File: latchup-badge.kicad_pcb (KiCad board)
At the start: 2 copper layers, 101.6 x 71.1 mm, 18 parts, among them U1 ICE40UP5K-SG48ITR, U2 TLV70012_SOT23-5, U3 TLV70033_SOT23-5

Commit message: Moar updates
Signed-off-by: Michael Welling <mwelling@ieee.org>
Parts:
- added C14: .1uF, Capacitor_SMD:C_0402_1005Metric, F.Cu at (144.1, 60.8)
- added C15: .1uF, Capacitor_SMD:C_0402_1005Metric, F.Cu at (130.8, 76.7)
- added R2: 10K, Resistor_SMD:R_0402_1005Metric, F.Cu at (141.5, 58.3)
- added U4: M25PX32-VMW, Package_SO:SOIJ-8_5.3x5.3mm_P1.27mm, F.Cu at (124.0, 79.2)
- added X1: ASE-12.000MHz, Oscillator:Oscillator_SMD_Abracon_ASE-4Pin_3.2x2.5mm, F.Cu at (141.2, 60.8)

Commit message: Add some artwork
Signed-off-by: Michael Welling <mwelling@ieee.org>
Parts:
- added G***: LOGO, latchup-badge:logo_1, F.Cu at (127.0, 104.1)
- added G***: LOGO, latchup-badge:logo, F.Cu at (127.0, 104.1)
- added J1: USB_B_Micro, Connector_USB:USB_Micro-B_Molex-105017-0001, B.Cu at (79.3, 78.2)
- added R3: 25, Resistor_SMD:R_0402_1005Metric, B.Cu at (85.0, 77.9)
- added R4: 25, Resistor_SMD:R_0402_1005Metric, B.Cu at (85.0, 78.9)
- added R5: 1.5K, Resistor_SMD:R_0402_1005Metric, B.Cu at (106.0, 68.3)
- C1, C10, C11, C12, C13, C14, C15, C2, C3, C4, C5, C6, C7, C8, C9, D1, R1, R2, U1, U2, U3, U4, X1: moved to B.Cu
- moved C8 43.3 mm to (98.0, 68.4), turned to 180 degrees
- moved C14 42.8 mm to (101.4, 59.9)
- moved C7 42.3 mm to (98.9, 65.6), turned to 180 degrees
- moved R2 37.5 mm to (104.0, 57.3), turned to 0 degrees
- moved C9 37.0 mm to (104.3, 65.7), turned to 180 degrees
- moved X1 37.0 mm to (104.3, 59.8), turned to 0 degrees
- moved C3 37.0 mm to (104.3, 63.8), turned to 0 degrees
- moved C10 37.0 mm to (104.3, 68.4), turned to 180 degrees
- moved R1 37.0 mm to (104.3, 67.4), turned to 180 degrees
- moved D1 30.1 mm to (107.7, 72.6)
- moved C5 29.8 mm to (93.3, 85.9), turned to 0 degrees
- moved U3 29.8 mm to (93.3, 82.7)
- moved C2 29.8 mm to (93.3, 79.5), turned to 0 degrees
- moved C6 27.1 mm to (109.2, 72.6)
- moved U1 23.4 mm to (111.1, 66.0), turned to 180 degrees
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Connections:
- U1 pad 14: Net-(U1-Pad14) -> /ICE40_SPI_SO
- U1 pad 15: Net-(U1-Pad15) -> /ICE40_SPI_SCK
- U1 pad 16: Net-(U1-Pad16) -> /ICE40_SPI_SS
- U1 pad 17: Net-(U1-Pad17) -> /ICE40_SPI_SI
- U4 pad 1: Net-(U4-Pad1) -> /ICE40_SPI_SS
- U4 pad 2: Net-(U4-Pad2) -> /ICE40_SPI_SI
- U4 pad 5: Net-(U4-Pad5) -> /ICE40_SPI_SO
- U4 pad 6: Net-(U4-Pad6) -> /ICE40_SPI_SCK
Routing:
- net +3V3: track 0.00 -> 1.74 mm, vias 0 -> 1
- added copper zone on F.Cu, net +3V3
- added copper zone on B.Cu, net GND
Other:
- board text added: "HELLO"
- board text added: "MY NAME IS"

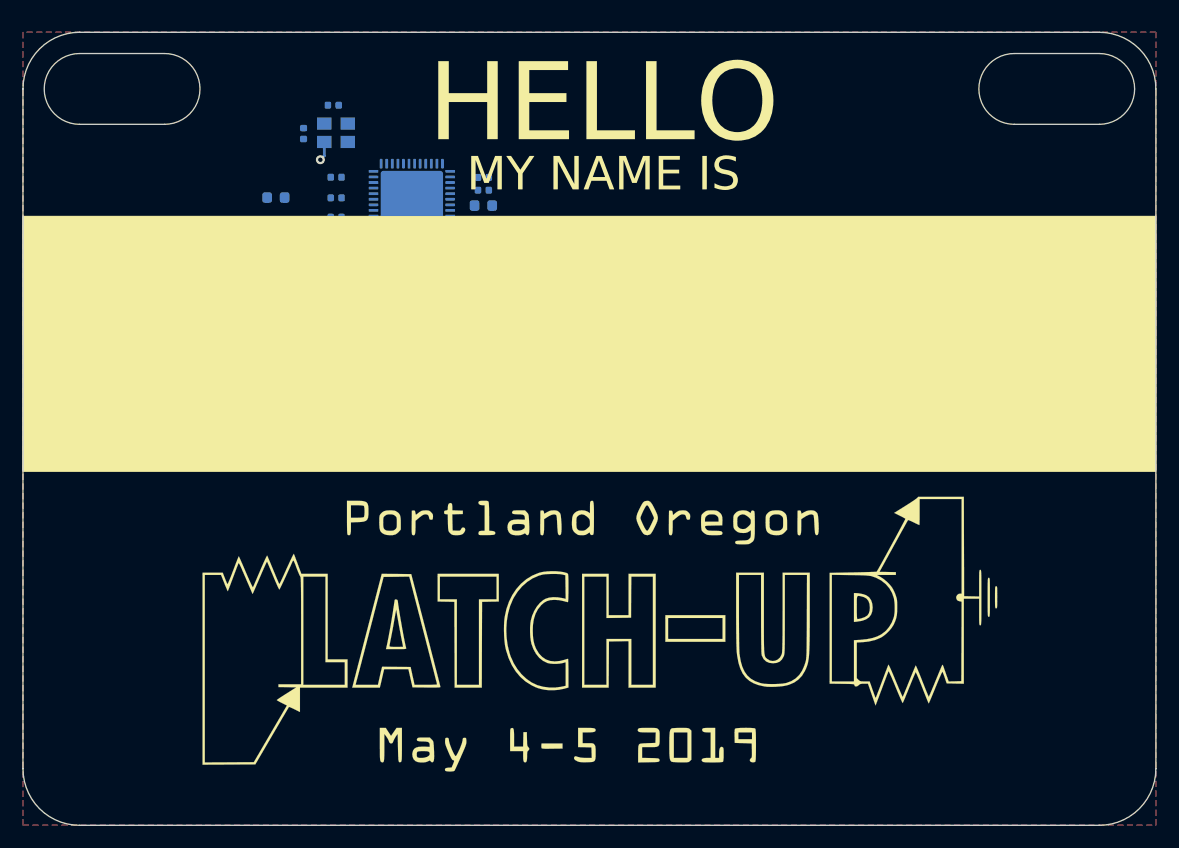
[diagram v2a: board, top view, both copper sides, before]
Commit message: Add some headers and route
Some small tweaks left but mostly done.

Signed-off-by: Michael Welling <mwelling@ieee.org>
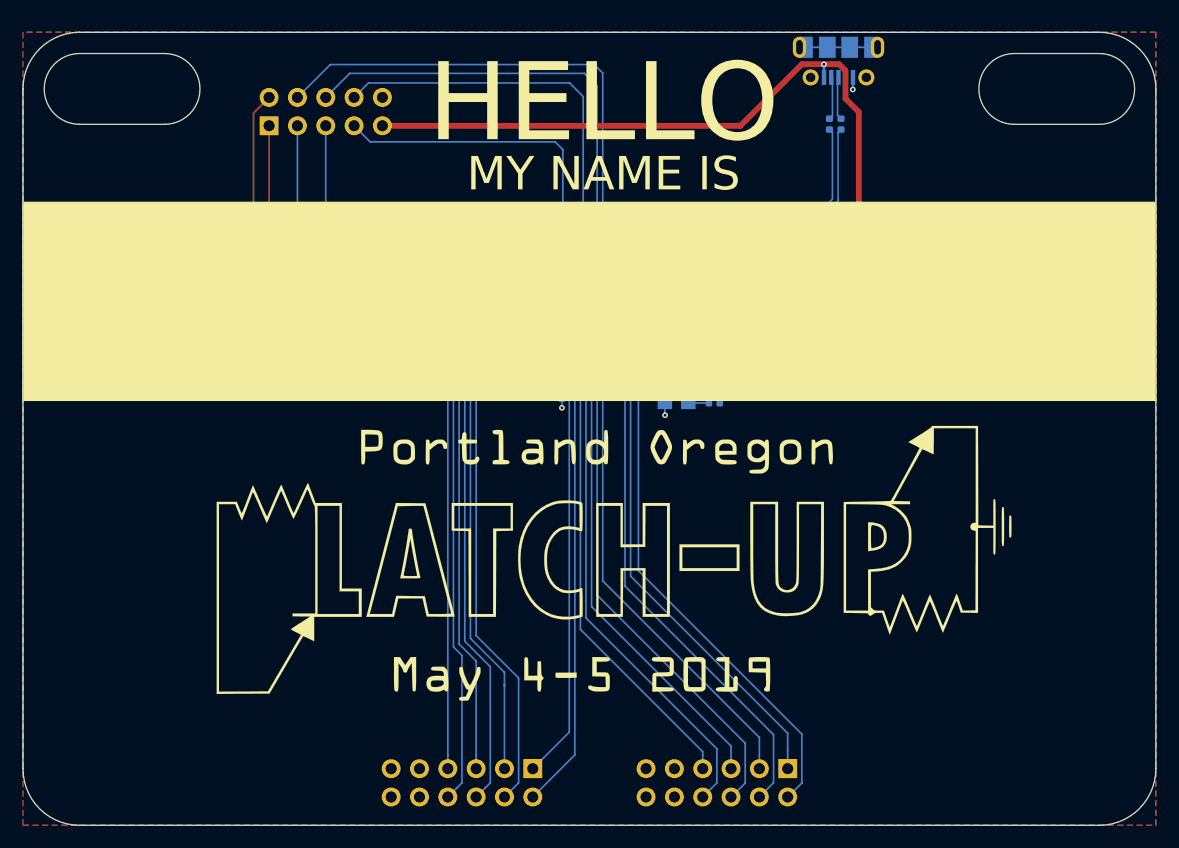
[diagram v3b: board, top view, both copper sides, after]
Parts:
- added J2: CONN_02X06, Connector_PinSocket_2.54mm:PinSocket_2x06_P2.54mm_Horizontal, B.Cu at (144.8, 116.8)
- added J3: CONN_02X06, Connector_PinSocket_2.54mm:PinSocket_2x06_P2.54mm_Horizontal, B.Cu at (121.9, 116.8)
- added J4: CONN_02X05, Connector_PinSocket_2.54mm:PinSocket_2x05_P2.54mm_Vertical, B.Cu at (98.3, 59.2)
- moved J1 74.3 mm to (149.3, 53.4), turned to 0 degrees
- moved R3 67.3 mm to (149.6, 59.0), turned to 90 degrees
- moved R4 66.6 mm to (148.5, 59.0), turned to 90 degrees
- moved C2 56.5 mm to (149.5, 73.8), turned to 270 degrees
- moved U3 53.7 mm to (146.3, 73.9), turned to 180 degrees
- moved C5 51.3 mm to (143.1, 73.9), turned to 270 degrees
- moved C1 49.9 mm to (149.5, 80.2), turned to 270 degrees
- moved U2 46.7 mm to (146.3, 80.3), turned to 180 degrees
- moved C4 43.9 mm to (143.1, 80.3), turned to 270 degrees
- moved R2 43.4 mm to (138.2, 84.0)
- moved C14 43.3 mm to (138.4, 82.4), turned to 180 degrees
- moved C7 42.1 mm to (139.3, 77.5), turned to 0 degrees
- moved C8 41.9 mm to (139.3, 75.6), turned to 0 degrees
- moved X1 38.5 mm to (134.8, 83.2), turned to 180 degrees
- moved C3 34.3 mm to (134.7, 79.5), turned to 180 degrees
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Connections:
- net Net-(R?1555303253-Pad1) renamed /USBD+
- net Net-(R?1555309571-Pad1) renamed /USBD-
- R5 pad 1: Net-(U1-Pad25) -> Net-(R5-Pad1)
- U1 pad 10: Net-(U1-Pad10) -> /J3_P6
- U1 pad 11: Net-(U1-Pad11) -> /J3_P5
- U1 pad 12: Net-(U1-Pad12) -> /J3_P8
- U1 pad 13: Net-(U1-Pad13) -> /J3_P7
- U1 pad 18: Net-(U1-Pad18) -> /RX
- U1 pad 19: Net-(U1-Pad19) -> /TX
- U1 pad 28: Net-(U1-Pad28) -> Net-(R5-Pad1)
- U1 pad 36: Net-(U1-Pad36) -> /J2_P2
- U1 pad 37: Net-(U1-Pad37) -> /J2_P1
- U1 pad 38: Net-(U1-Pad38) -> /J2_P4
- U1 pad 42: Net-(U1-Pad42) -> /J2_P3
- U1 pad 43: Net-(U1-Pad43) -> /J2_P6
- U1 pad 44: Net-(U1-Pad44) -> /J2_P5
- U1 pad 45: Net-(U1-Pad45) -> /J2_P8
- U1 pad 46: Net-(U1-Pad46) -> /J2_P7
- U1 pad 47: Net-(U1-Pad47) -> /J3_P2
- U1 pad 48: Net-(U1-Pad48) -> /J3_P1
- U1 pad 6: Net-(U1-Pad6) -> /J3_P4
- U1 pad 7: Net-(U1-Pad7) -> /CDONE
- U1 pad 8: Net-(U1-Pad8) -> /CRESET
- U1 pad 9: Net-(U1-Pad9) -> /J3_P3
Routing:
- net +5V: track 0.00 -> 80.2 mm, vias 0 -> 5
- net /J3_P8: track 0.00 -> 54.4 mm
- net /J3_P6: track 0.00 -> 53.0 mm
- net /J3_P7: track 0.00 -> 52.9 mm
- net /J3_P5: track 0.00 -> 50.6 mm
- net /J3_P4: track 0.00 -> 50.6 mm
- net /J3_P3: track 0.00 -> 49.4 mm
- net /TX: track 0.00 -> 49.0 mm
- net /CDONE: track 0.00 -> 48.3 mm, vias 0 -> 1
- net /ICE40_SPI_SI: track 0.00 -> 45.8 mm
- net /J2_P2: track 0.00 -> 45.3 mm
- net /RX: track 0.00 -> 44.6 mm
- net /J2_P4: track 0.00 -> 44.0 mm
- net /J2_P6: track 0.00 -> 44.0 mm
- net /CRESET: track 0.00 -> 43.4 mm, vias 0 -> 1
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- added copper zone on B.Cu, net +3V3
- added copper zone on F.Cu, net GND
- removed copper zone on F.Cu, net +3V3
- removed copper zone on B.Cu, net GND
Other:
- net class Default: clearance 0.2 -> 0.1524; trace_width 0.25 -> 0.1524; via_dia 0.8 -> 0.508; via_drill 0.4 -> 0.254
- rule trace_clearance: 0.2 -> 0.1524
- rule trace_min: 0.2 -> 0.1524
- rule via_min_drill: 0.3 -> 0.254
- rule via_min_size: 0.4 -> 0.508

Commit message: OSHPark is sponsoring the PCBs!
Signed-off-by: Michael Welling <mwelling@ieee.org>
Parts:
- added G***: LOGO, latchup-badge:logo_3, B.Cu at (106.9, 101.8)
- added G***: KiCad Logo, latchup-badge:KiCad-Logo_Copper_11mmx5mm, F.Cu at (90.6, 117.9)
- added G***: LOGO, latchup-badge:logo_2, B.Cu at (159.0, 102.2)
- added R6: 10K, Resistor_SMD:R_0402_1005Metric, B.Cu at (98.2, 62.5)
- added R7: 10K, Resistor_SMD:R_0402_1005Metric, B.Cu at (124.2, 64.8)
- added R8: 10K, Resistor_SMD:R_0402_1005Metric, B.Cu at (114.2, 68.4)
- added R9: 10K, Resistor_SMD:R_0402_1005Metric, B.Cu at (126.8, 69.2)
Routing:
- net /CRESET: track 43.4 -> 46.3 mm
- net Net-(R8-Pad1): track 0.00 -> 2.61 mm
- net Net-(R9-Pad1): track 0.00 -> 2.15 mm
- net /RX: track 44.6 -> 46.3 mm
- net /TX: track 49.0 -> 50.5 mm
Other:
- board text added: "PCB Sponsored by:"
- board text added: "m_w"

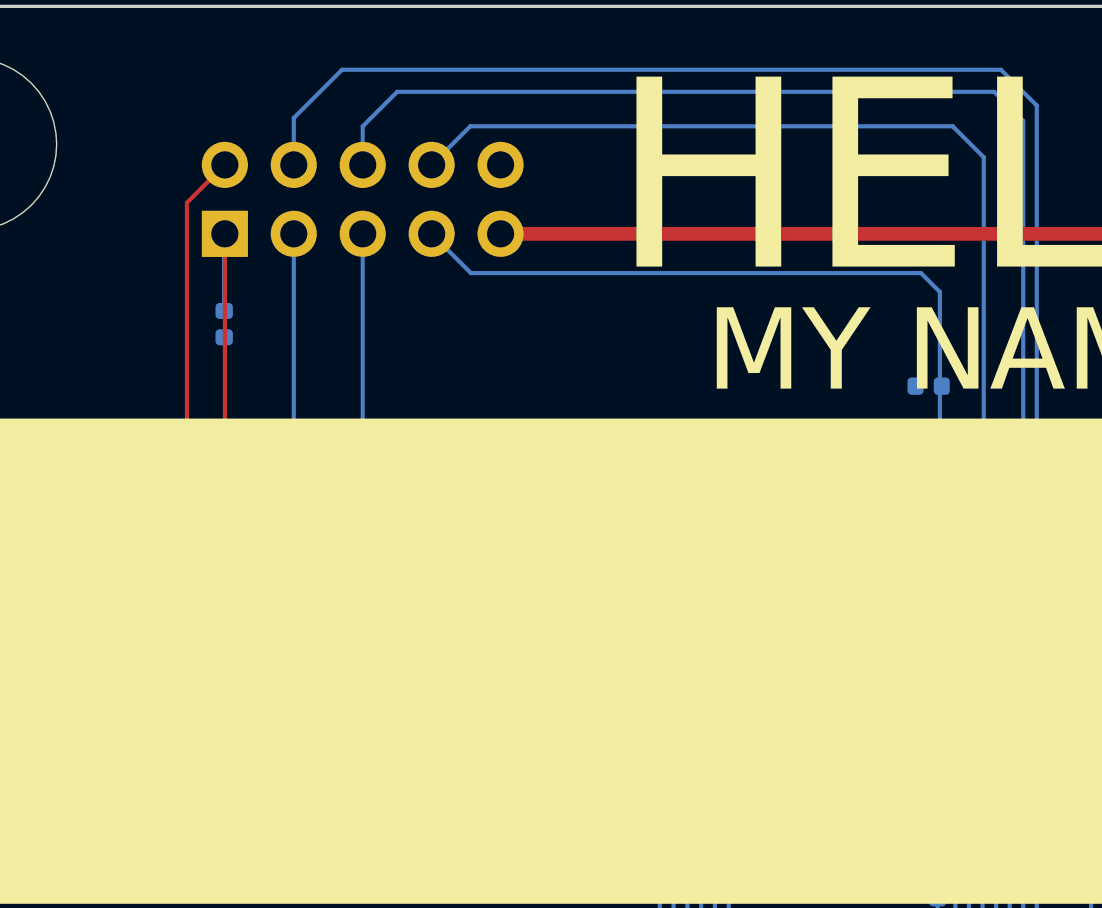
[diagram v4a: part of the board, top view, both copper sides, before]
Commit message: Tweak routing per review from tnt
Gives the GND plane more room to breathe.

Signed-off-by: Michael Welling <mwelling@ieee.org>
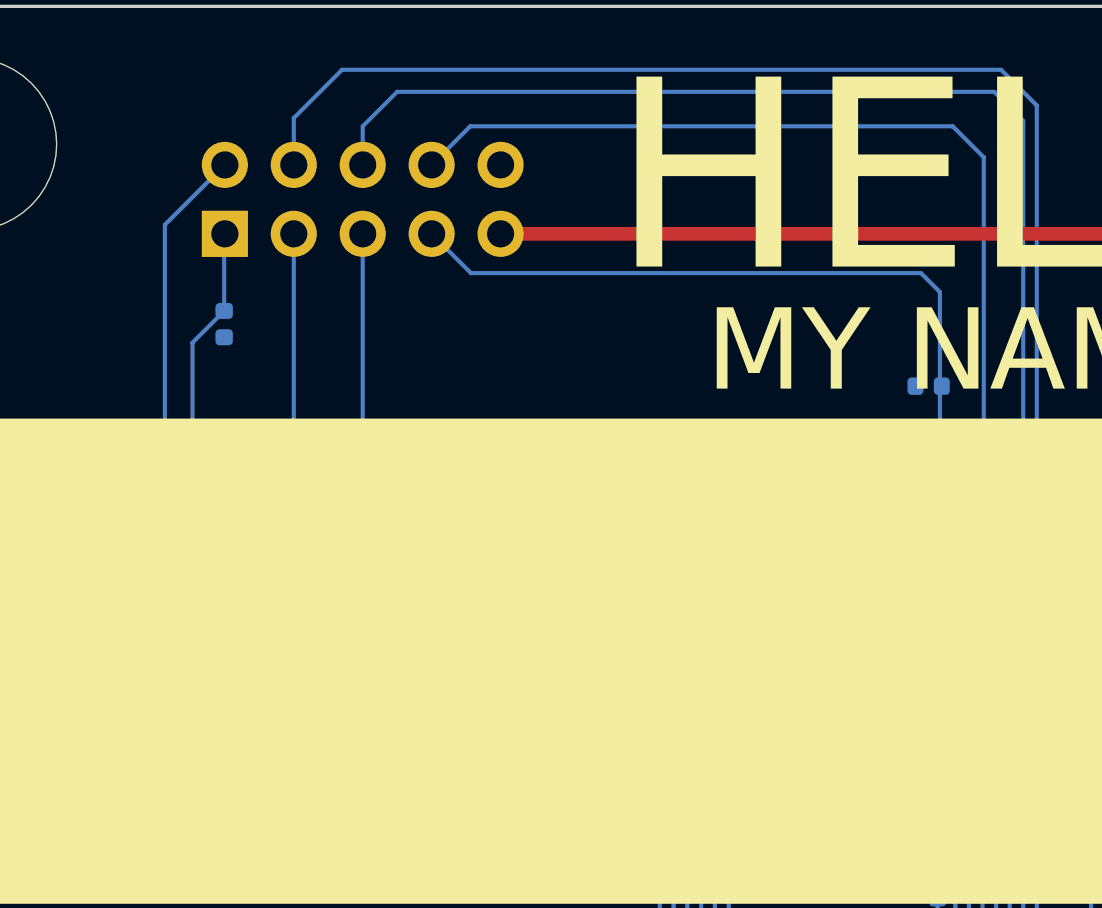
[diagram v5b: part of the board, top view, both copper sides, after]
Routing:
- net /CRESET: track 46.3 -> 42.8 mm, vias 1 -> 2
- net /CDONE: track 48.3 -> 47.2 mm, vias 1 -> 2
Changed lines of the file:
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@@
     (thickness 1.6)
     (drawings 21)
-    (tracks 328)
+    (tracks 334)
     (zones 0)
     (modules 39)
@@
   (segment (start 100.8126 54.9148) (end 102.5906 53.1368) (width 0.1524) (layer "B.Cu") (net 51))
   (segment (start 100.8126 56.642) (end 100.8126 54.9148) (width 0.1524) (layer "B.Cu") (net 51))
-  (via (at 123.0122 77.761554) (size 0.508) (drill 0.254) (layers "F.Cu" "B.Cu") (net 52))
-  (segment (start 124.486971 77.761554) (end 123.0122 77.761554) (width 0.1524) (layer "B.Cu") (net 52))
-  (segment (start 124.504371 77.744154) (end 124.486971 77.761554) (width 0.1524) (layer "B.Cu") (net 52))
-  (segment (start 96.8756 58.039) (end 97.422601 57.491999) (width 0.1524) (layer "F.Cu") (net 52))
-  (segment (start 97.422601 57.491999) (end 98.2726 56.642) (width 0.1524) (layer "F.Cu") (net 52))
-  (segment (start 96.8756 76.0476) (end 96.8756 58.039) (width 0.1524) (layer "F.Cu") (net 52))
-  (segment (start 98.589554 77.761554) (end 96.8756 76.0476) (width 0.1524) (layer "F.Cu") (net 52))
-  (segment (start 123.0122 77.761554) (end 98.589554 77.761554) (width 0.1524) (layer "F.Cu") (net 52))
-  (via (at 123.4694 77.2668) (size 0.508) (drill 0.254) (layers "F.Cu" "B.Cu") (net 53))
-  (segment (start 123.492046 77.244154) (end 123.4694 77.2668) (width 0.1524) (layer "B.Cu") (net 53))
-  (segment (start 124.504371 77.244154) (end 123.492046 77.244154) (width 0.1524) (layer "B.Cu") (net 53))
-  (segment (start 98.2726 75.692) (end 98.2726 59.182) (width 0.1524) (layer "F.Cu") (net 53))
-  (segment (start 99.5426 76.962) (end 98.2726 75.692) (width 0.1524) (layer "F.Cu") (net 53))
-  (segment (start 123.1646 76.962) (end 99.5426 76.962) (width 0.1524) (layer "F.Cu") (net 53))
-  (segment (start 123.4694 77.2668) (end 123.1646 76.962) (width 0.1524) (layer "F.Cu") (net 53))
+  (segment (start 124.486971 77.761554) (end 124.504371 77.744154) (width 0.1524) (layer "B.Cu") (net 52))
+  (segment (start 116.904046 77.761554) (end 124.486971 77.761554) (width 0.1524) (layer "B.Cu") (net 52))
+  (via (at 116.904046 77.761554) (size 0.508) (drill 0.254) (layers "F.Cu" "B.Cu") (net 52))
+  (via (at 112.903 73.7362) (size 0.508) (drill 0.254) (layers "F.Cu" "B.Cu") (net 52))
+  (segment (start 116.904046 77.761554) (end 112.903 73.760508) (width 0.1524) (layer "F.Cu") (net 52))
+  (segment (start 112.54379 73.7362) (end 112.903 73.7362) (width 0.1524) (layer "B.Cu") (net 52))
+  (segment (start 112.903 73.760508) (end 112.903 73.7362) (width 0.1524) (layer "F.Cu") (net 52))
+  (segment (start 98.2726 56.642) (end 96.0628 58.8518) (width 0.1524) (layer "B.Cu") (net 52))
+  (segment (start 96.0628 58.8518) (end 96.0628 72.2122) (width 0.1524) (layer "B.Cu") (net 52))
+  (segment (start 97.5868 73.7362) (end 112.54379 73.7362) (width 0.1524) (layer "B.Cu") (net 52))
+  (segment (start 96.0628 72.2122) (end 97.5868 73.7362) (width 0.1524) (layer "B.Cu") (net 52))
   (segment (start 98.2472 59.2074) (end 98.2726 59.182) (width 0.1524) (layer "B.Cu") (net 53))
   (segment (start 98.2472 62.0244) (end 98.2472 59.2074) (width 0.1524) (layer "B.Cu") (net 53))
+  (segment (start 124.504371 77.244154) (end 117.573846 77.244154) (width 0.1524) (layer "B.Cu") (net 53))
+  (segment (start 117.573846 77.244154) (end 117.5512 77.2668) (width 0.1524) (layer "B.Cu") (net 53))
+  (via (at 117.5512 77.2668) (size 0.508) (drill 0.254) (layers "F.Cu" "B.Cu") (net 53))
+  (via (at 113.3856 73.1012) (size 0.508) (drill 0.254) (layers "F.Cu" "B.Cu") (net 53))
+  (segment (start 117.5512 77.2668) (end 113.3856 73.1012) (width 0.1524) (layer "F.Cu") (net 53))
+  (segment (start 113.02639 73.1012) (end 113.3856 73.1012) (width 0.1524) (layer "B.Cu") (net 53))
+  (segment (start 98.4758 73.1012) (end 113.02639 73.1012) (width 0.1524) (layer "B.Cu") (net 53))
+  (segment (start 97.0788 71.7042) (end 98.4758 73.1012) (width 0.1524) (layer "B.Cu") (net 53))
+  (segment (start 97.0788 63.1928) (end 97.0788 71.7042) (width 0.1524) (layer "B.Cu") (net 53))
+  (segment (start 98.2472 62.0244) (end 97.0788 63.1928) (width 0.1524) (layer "B.Cu") (net 53))
   (segment (start 117.31496 68.3768) (end 117.32004 68.38188) (width 0.1524) (layer "B.Cu") (net 54))
   (segment (start 114.7088 68.3768) (end 117.31496 68.3768) (width 0.1524) (layer "B.Cu") (net 54))
